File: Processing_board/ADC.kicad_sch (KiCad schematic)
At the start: 10 parts, among them IC2 REF5025AQDRQ1, IC5 OPA192IDR, U3 ADS7953SBDBT

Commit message: the 2nd (hopefully final) version of circuit diagram
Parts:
- added R7: 10k, symbol Device:R
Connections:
- net *CS: now also R7.2
- net 3.3V: now also R7.1
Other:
- note added: "Pull-up"
- note removed: "If using SPI protocol, does SDI = MOSI, SDO = MISO and SCLCK = SCK ?"
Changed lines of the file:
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@@
-		)
-	)
-	(text "If using SPI protocol, does SDI = MOSI, SDO = MISO\nand SCLCK = SCK ?"
-		(exclude_from_sim no)
-		(at 249.174 61.976 0)
-		(effects
-			(font
-				(size 1.27 1.27)
-			)
 		)
 	)
@@
 		(exclude_from_sim no)
 		(at 63.246 145.034 0)
+		(effects
+			(font
+				(size 1.27 1.27)
+			)
+		)
+	)
+	(text "Pull-up\n"
+		(exclude_from_sim no)
+		(at 232.41 58.42 90)
 		(effects
 			(font
@@
 	)
 	(junction
+		(at 234.95 71.12)
+		(diameter 0)
+		(color 0 0 0 0)
+	)
+	(junction
 		(at 203.2 76.2)
 		(diameter 0)
@@
 	(wire
 		(pts
-			(xy 212.09 71.12) (xy 214.63 71.12)
+			(xy 212.09 71.12) (xy 234.95 71.12)
 		)
 		(stroke
@@
 	(wire
 		(pts
+			(xy 234.95 62.23) (xy 234.95 71.12)
+		)
+		(stroke
+			(width 0)
+			(type default)
+		)
+	)
+	(wire
+		(pts
 			(xy 196.85 71.12) (xy 203.2 71.12)
 		)
@@
 	(wire
 		(pts
-			(xy 212.09 69.85) (xy 212.09 71.12)
+			(xy 212.09 71.12) (xy 212.09 69.85)
+		)
+		(stroke
+			(width 0)
+			(type default)
+		)
+	)
+	(wire
+		(pts
+			(xy 234.95 71.12) (xy 246.38 71.12)
 		)
 		(stroke
@@
 		(pts
 			(xy 58.42 114.3) (xy 100.33 114.3)
+		)
+		(stroke
+			(width 0)
+			(type default)
+		)
+	)
+	(wire
+		(pts
+			(xy 234.95 49.53) (xy 234.95 54.61)
 		)
 		(stroke
@@
 		)
 	)
+	(global_label "3.3V"
+		(shape input)
+		(at 234.95 49.53 90)
+		(fields_autoplaced yes)
+		(effects
+			(font
+				(size 1.27 1.27)
+			)
+			(justify left)
+		)
+		(property "Intersheetrefs" "${INTERSHEET_REFS}"
+			(at 234.95 42.4324 90)
+			(effects
+				(font
+					(size 1.27 1.27)
+				)
+				(justify left)
+				(hide yes)
+			)
+		)
+	)
 	(global_label "5V"
 		(shape input)
@@
 	(hierarchical_label "*CS"
 		(shape input)
-		(at 214.63 71.12 0)
+		(at 246.38 71.12 0)
 		(effects
 			(font
@@
 					(unit 1)
 				)
+			)
+		)
+	)
+	(symbol
+		(lib_id "Device:R")
+		(at 234.95 58.42 0)
+		(unit 1)
+		(exclude_from_sim no)
+		(in_bom yes)
+		(on_board yes)
+		(dnp no)
+		(fields_autoplaced yes)
+		(property "Reference" "R7"
+			(at 237.49 57.1499 0)
+			(effects
+				(font
+					(size 1.27 1.27)
+				)
+				(justify left)
+			)
+		)
+		(property "Value" "10k"
+			(at 237.49 59.6899 0)
+			(effects
+				(font
+					(size 1.27 1.27)
+				)
+				(justify left)
+			)
+		)
+		(property "Footprint" ""
+			(at 233.172 58.42 90)
+			(effects
+				(font
+					(size 1.27 1.27)
+				)
+				(hide yes)
+			)
+		)
+		(property "Datasheet" "~"
+			(at 234.95 58.42 0)
+			(effects
+				(font
+					(size 1.27 1.27)
+				)
+				(hide yes)
+			)
+		)
+		(property "Description" "Resistor"
+			(at 234.95 58.42 0)
+			(effects
+				(font
+					(size 1.27 1.27)
+				)
+				(hide yes)
+			)
+		)
+		(pin "1"
+		)
+		(pin "2"
+		)
+		(instances
+			(project ""
+				(path "/b48cfd4a-6c36-4270-b2b4-45cb26e35477/81fcf985-d5d5-4bbe-9990-9ad1ad945323"
+					(reference "R7")
+					(unit 1)
+				)

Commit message: added reset button
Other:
- company: (none) -> N-Pulse
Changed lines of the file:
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@@
 	(generator_version "9.0")
 	(paper "A4")
+	(title_block
+		(company "N-Pulse")
+	)
 	(text "AGND, BDGND, AINM, REFM pins have to be\nconnected to the same GND (copper fill area)\n"
 		(exclude_from_sim no)

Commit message: addressed all reviews except the LDO 5V
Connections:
- net GPIO2: now reaches U3.1 (GPIO2)
- net GPIO3: now reaches U3.2 (GPIO3)
- net MXO: no longer names the net of IC5.3 (+IN), U3.7 (MXO)
- no-connect marks 0 -> 2
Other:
- note added: "AINP"
- note added: "GPIO2 and GPIO3 are connected to PB1 and PB2 of STM32 (not crucial, for debug or else)"
- note added: "GPIO2 pin can also control ADC range (0-5V or 0-2.5V)"
- note added: "GPIO3 can also also be used for power-down function"
- note added: "MXO"

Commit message: 3 RF antennas
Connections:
- net 3.3V: no longer C30.1, C32.1, C33.2, IC2.2 (VIN), U3.29 (VA+), U3.36 (VBD+), U3.5 (VA+)
- net 5V renamed +5V
- new net +3.3V: C30.1, C32.1, C33.2, IC2.2 (VIN), U3.29 (VA+), U3.36 (VBD+), U3.5 (VA+)
- no-connect marks 2 -> 8

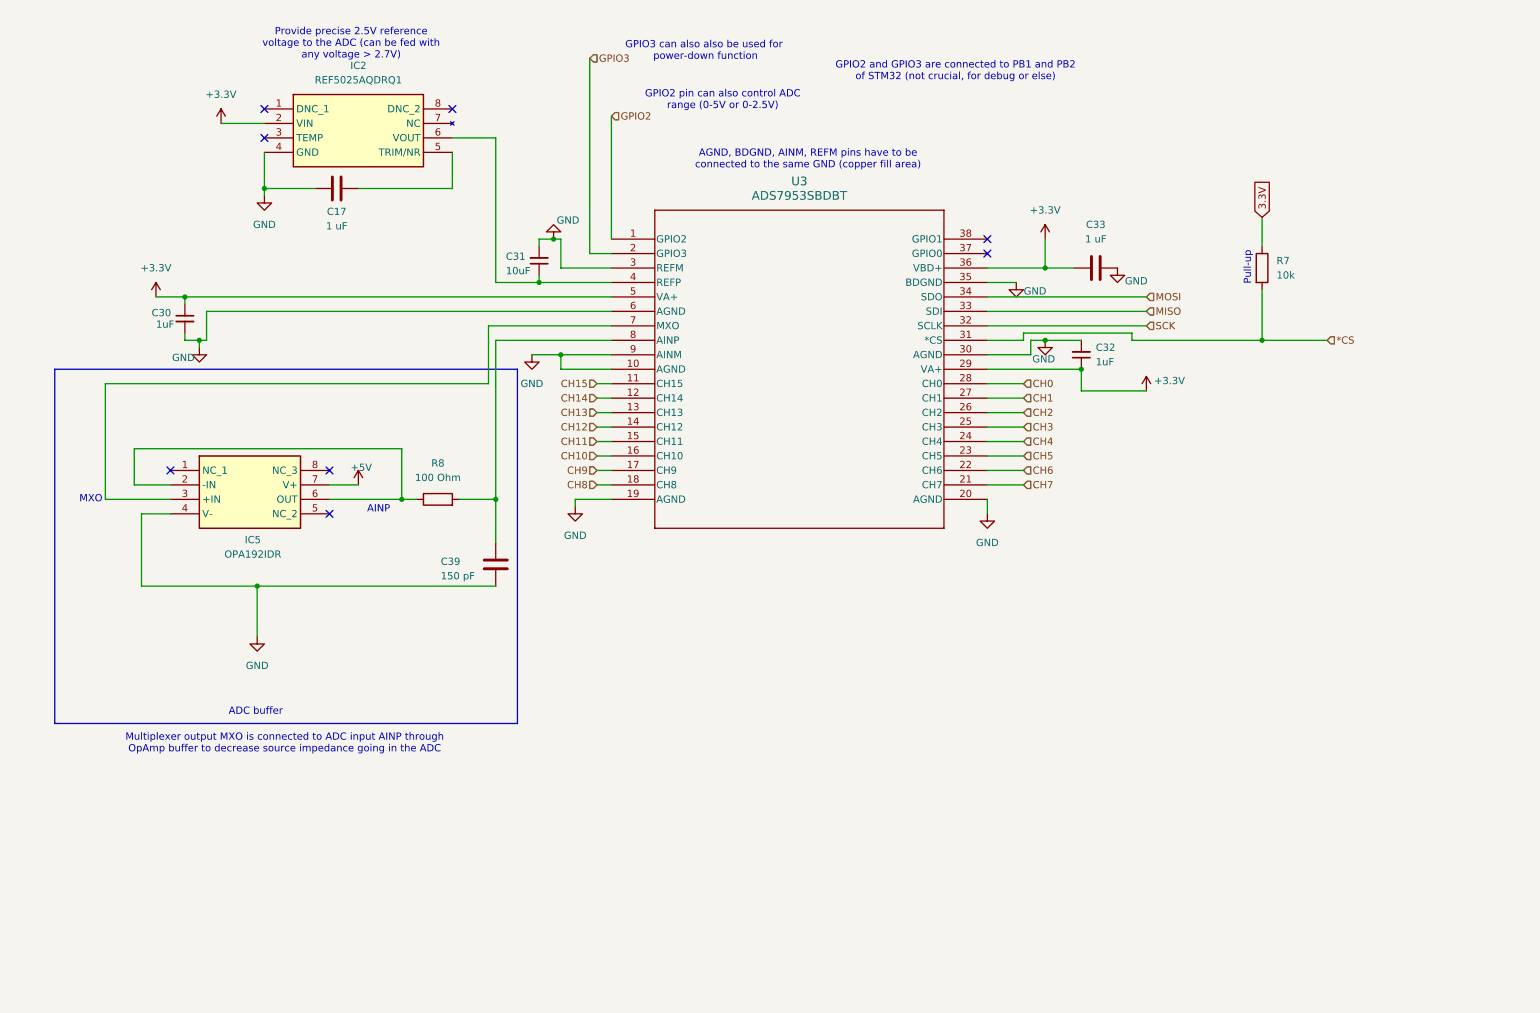
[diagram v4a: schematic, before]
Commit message: added all footprints, ready (?) to design PCB
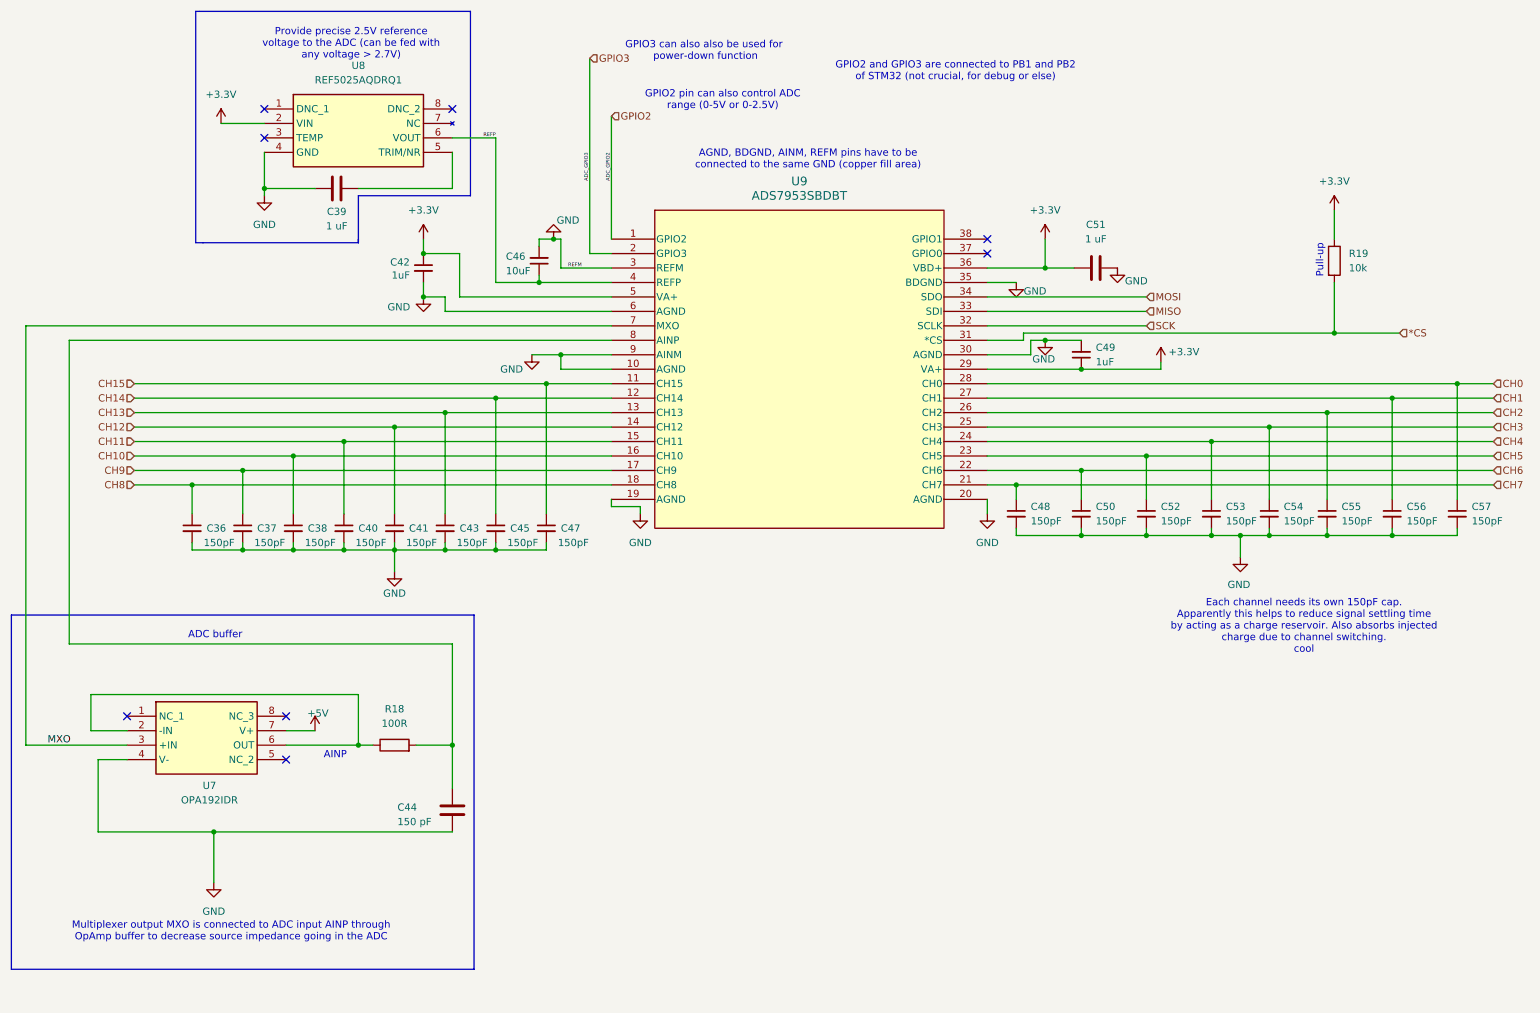
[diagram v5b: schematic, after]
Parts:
- added C36, C37, C38, C40, C41, C43, C45, C47, C48, C50, C52, C53, C54, C55, C56, C57: 150pF, Capacitor_SMD:C_0402_1005Metric, symbol Device:C_Small
- C39: renamed from C17; footprint (none) -> Capacitor_SMD:C_0402_1005Metric
- C42: renamed from C30; footprint (none) -> Capacitor_SMD:C_0402_1005Metric
- C44: renamed from C39; footprint (none) -> Capacitor_SMD:C_0402_1005Metric
- C46: renamed from C31; footprint (none) -> Capacitor_SMD:C_0402_1005Metric
- C49: renamed from C32; footprint (none) -> Capacitor_SMD:C_0402_1005Metric
- C51: renamed from C33; footprint (none) -> Capacitor_SMD:C_0402_1005Metric
- R18: renamed from R8; value 100 Ohm -> 100R; footprint (none) -> Resistor_SMD:R_0402_1005Metric
- R19: renamed from R7; footprint (none) -> Resistor_SMD:R_0402_1005Metric
- U7: renamed from IC5; footprint SOIC127P600X175-8N -> OPA192IDR:SOIC127P600X175-8N
- U8: renamed from IC2; footprint SOIC127P600X175-8N -> REF5025AQDRQ1:SOIC127P600X175-8N
- U9: renamed from U3; footprint DBT38 -> ADS7953SBDBT:DBT38
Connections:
- net 3.3V is gone; now on net +3.3V: R19.1
- net CH0: now also C57.1
- net CH1: now also C56.1
- net CH10: now also C38.1
- net CH11: now also C40.1
- net CH12: now also C41.1
- net CH13: now also C43.1
- net CH14: now also C45.1
- net CH15: now also C47.1
- net CH2: now also C55.1
- net CH3: now also C54.1
- net CH4: now also C53.1
- net CH5: now also C52.1
- net CH6: now also C50.1
- net CH7: now also C48.1
- net CH8: now also C36.1
- net CH9: now also C37.1
- net GND: now also C36.2, C37.2, C38.2, C40.2, C41.2, C43.2, C45.2, C47.2, C48.2, C50.2, C52.2, C53.2, C54.2, C55.2, C56.2, C57.2
- net REFP: now reaches C46.1, U8.6 (VOUT), U9.4 (REFP)
- net MXO: now reaches U7.3 (+IN), U9.7 (MXO)
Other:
- note added: "Each channel needs its own 150pF cap. Apparently this helps to reduce signal settling time by acting as a charge reservoir. Also absorbs injected charge due to channel switching. cool"
- note removed: "MXO"
- moved on the sheet: C42, C44, R18, R19, U7

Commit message: first draft of PCB almost done
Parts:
- added C38: 1uF, Capacitor_SMD:C_0402_1005Metric, symbol Device:C
- C35: renamed from C39; value 1 uF -> 1uF
- renumbered C36 to C34, C37 to C36, C38 to C37, C40 to C39, C41 to C40, C42 to C41, C43 to C42, C44 to C43, C45 to C44, C46 to C45, C47 to C46, C48 to C47, C49 to C48, C50 to C49, C51 to C50, C52 to C51, C53 to C52, C54 to C53, C55 to C54, C56 to C55, C57 to C56
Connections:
- net +3.3V: now also C35.1
- net GND: now also C38.1
- net at U8.5 (TRIM/NR): now also C38.2; no longer C35.1
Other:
- moved on the sheet: C35

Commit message: more minor cleanup
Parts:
- added TP10, TP7, TP9: PN5260, PN5260:PN5260, symbol PN5260:5260
- added TP11, TP12, TP8: TestPoint, TestPoint:TestPoint_Pad_D1.0mm, symbol Connector:TestPoint
- renumbered R18 to R17, R19 to R18
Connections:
- net *CS: now also TP12.1
- net GND: now also TP7.1
- net MISO: now also TP10.1
- net MOSI: now also TP9.1
- net SCK: now also TP11.1
- net at C43.1, R17.2, U9.8 (AINP): now also TP8.1
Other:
- note added: "(Test point is just to have convenient GND point on right side of board)"
- moved on the sheet: R17

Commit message: more cleanup
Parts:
- renumbered C51 to C101, C52 to C103, C53 to C104, C54 to C107, C55 to C108, C56 to C110, C34 to C58, C35 to C60, C36 to C62, C37 to C63, C38 to C64, C39 to C65, C40 to C67, C41 to C68, C42 to C69, C43 to C70, C44 to C72, C45 to C76, C46 to C77, C47 to C93, C48 to C96, C49 to C97, C50 to C99, R17 to R25, R18 to R36, TP7 to TP14, TP8 to TP15, TP9 to TP22, TP10 to TP23, TP11 to TP24, TP12 to TP25, U7 to U10, U8 to U11, U9 to U14
